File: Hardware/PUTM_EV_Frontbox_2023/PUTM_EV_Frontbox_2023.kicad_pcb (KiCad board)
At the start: 4 copper layers, 75 x 75 mm, 201 parts, among them IC1 ELVH-MF12D-HRRJ-C-N3A4, IC2 ELVH-MF12D-HRRJ-C-N3A4, J2 Conn_01x04, J5 Conn_02x14_Counter_Clockwise, K1 UMS05-1A80-75D, Q1 NX7002AK, SW1 Reset switch, U1 STM32G473RCTx, U10 TLP291-4, U11 TLP291-4, U12 TLV9152IDDFR, U17 MCP6002-xMC, U18 MCP6N11-005, U19 TLV743P, U2 MCP6002-xMC, U20 LM4040DBZ-5, U21 MCP6001, U22 MCP6N11-005, U23 MCP6001, U3 IMS330DHCX, U4 TLV743P, U5 TLV743P, U6 BD50FC0FP, U7 LM62440-Q1, U8 MCP2542FDxMF, Y1 ABM8G-48.000MHZ

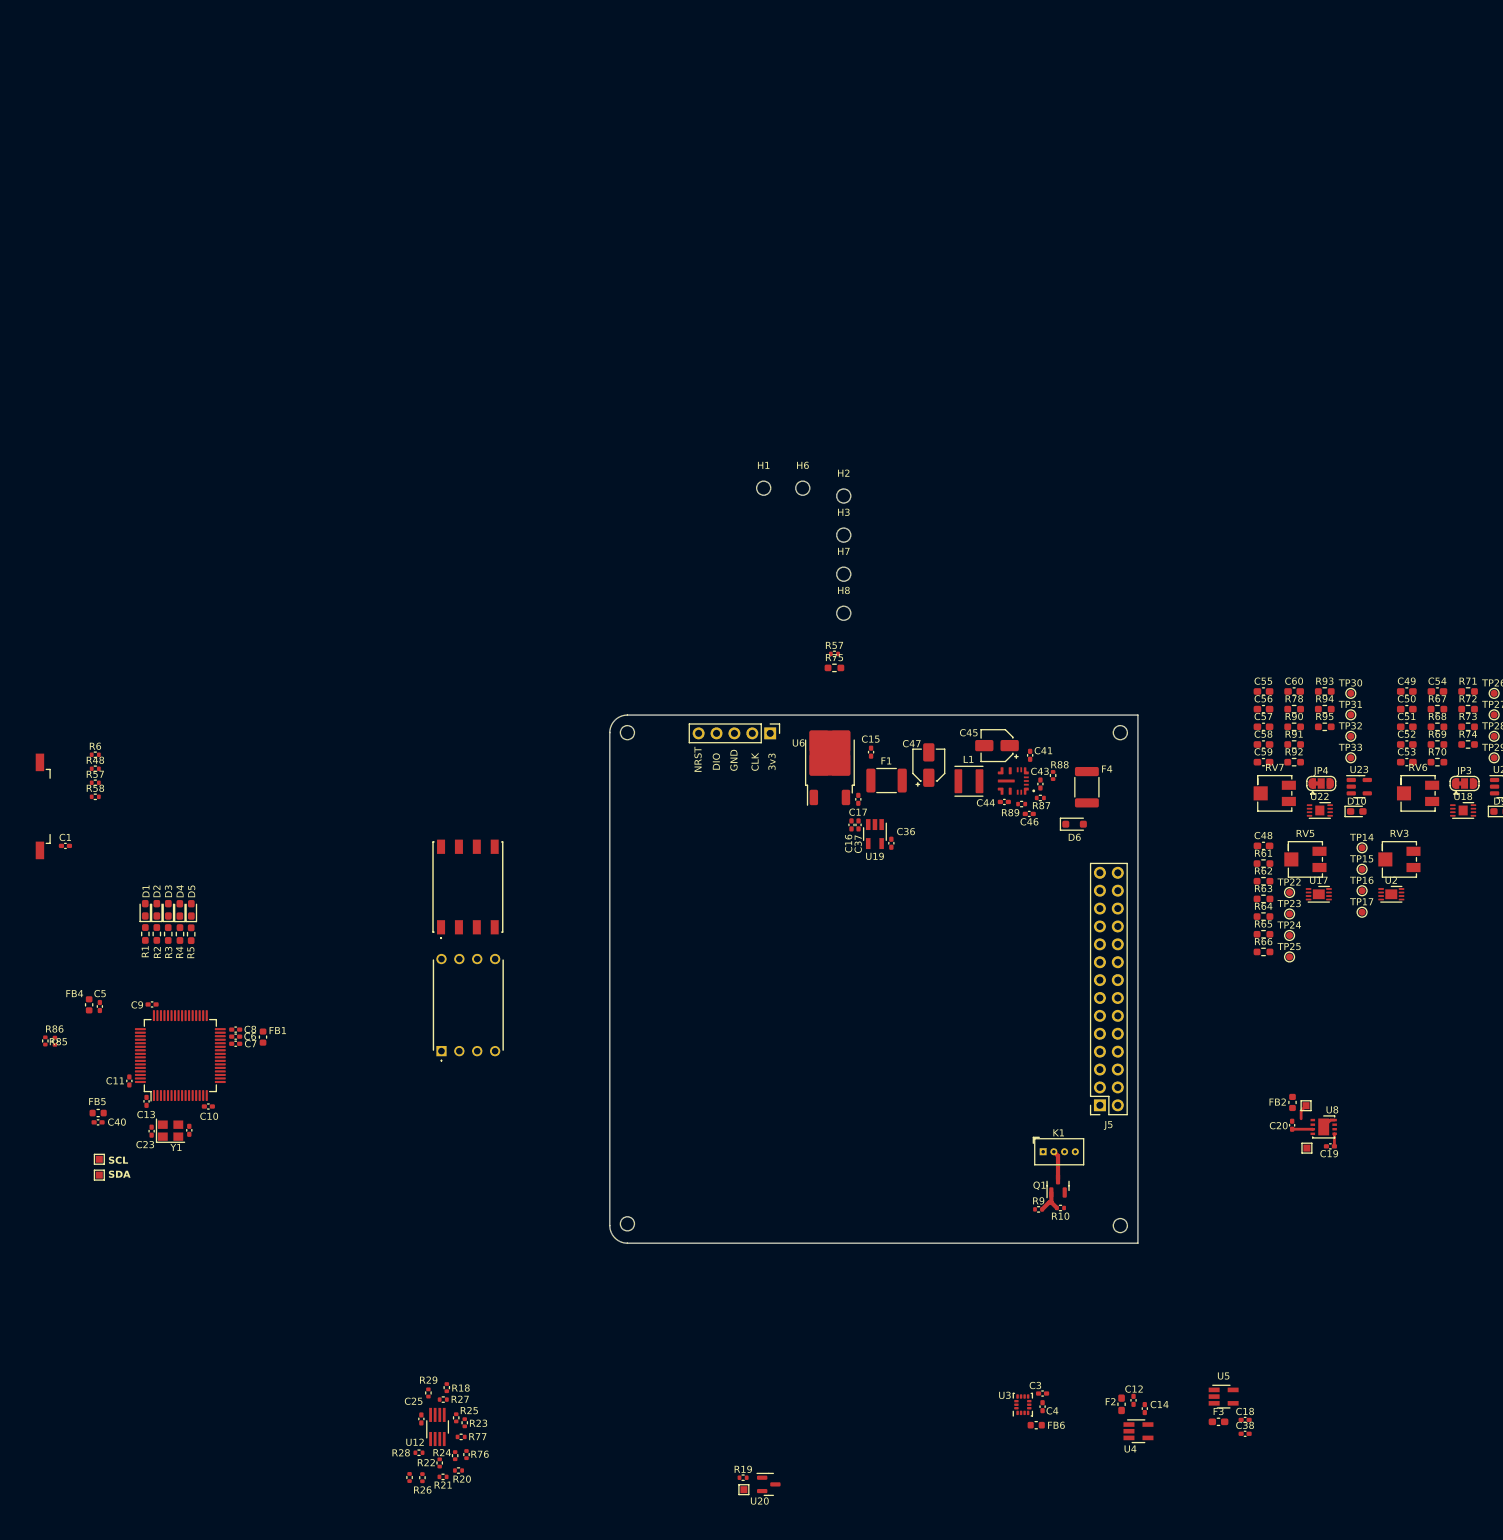
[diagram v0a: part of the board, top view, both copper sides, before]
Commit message: Schematic updates
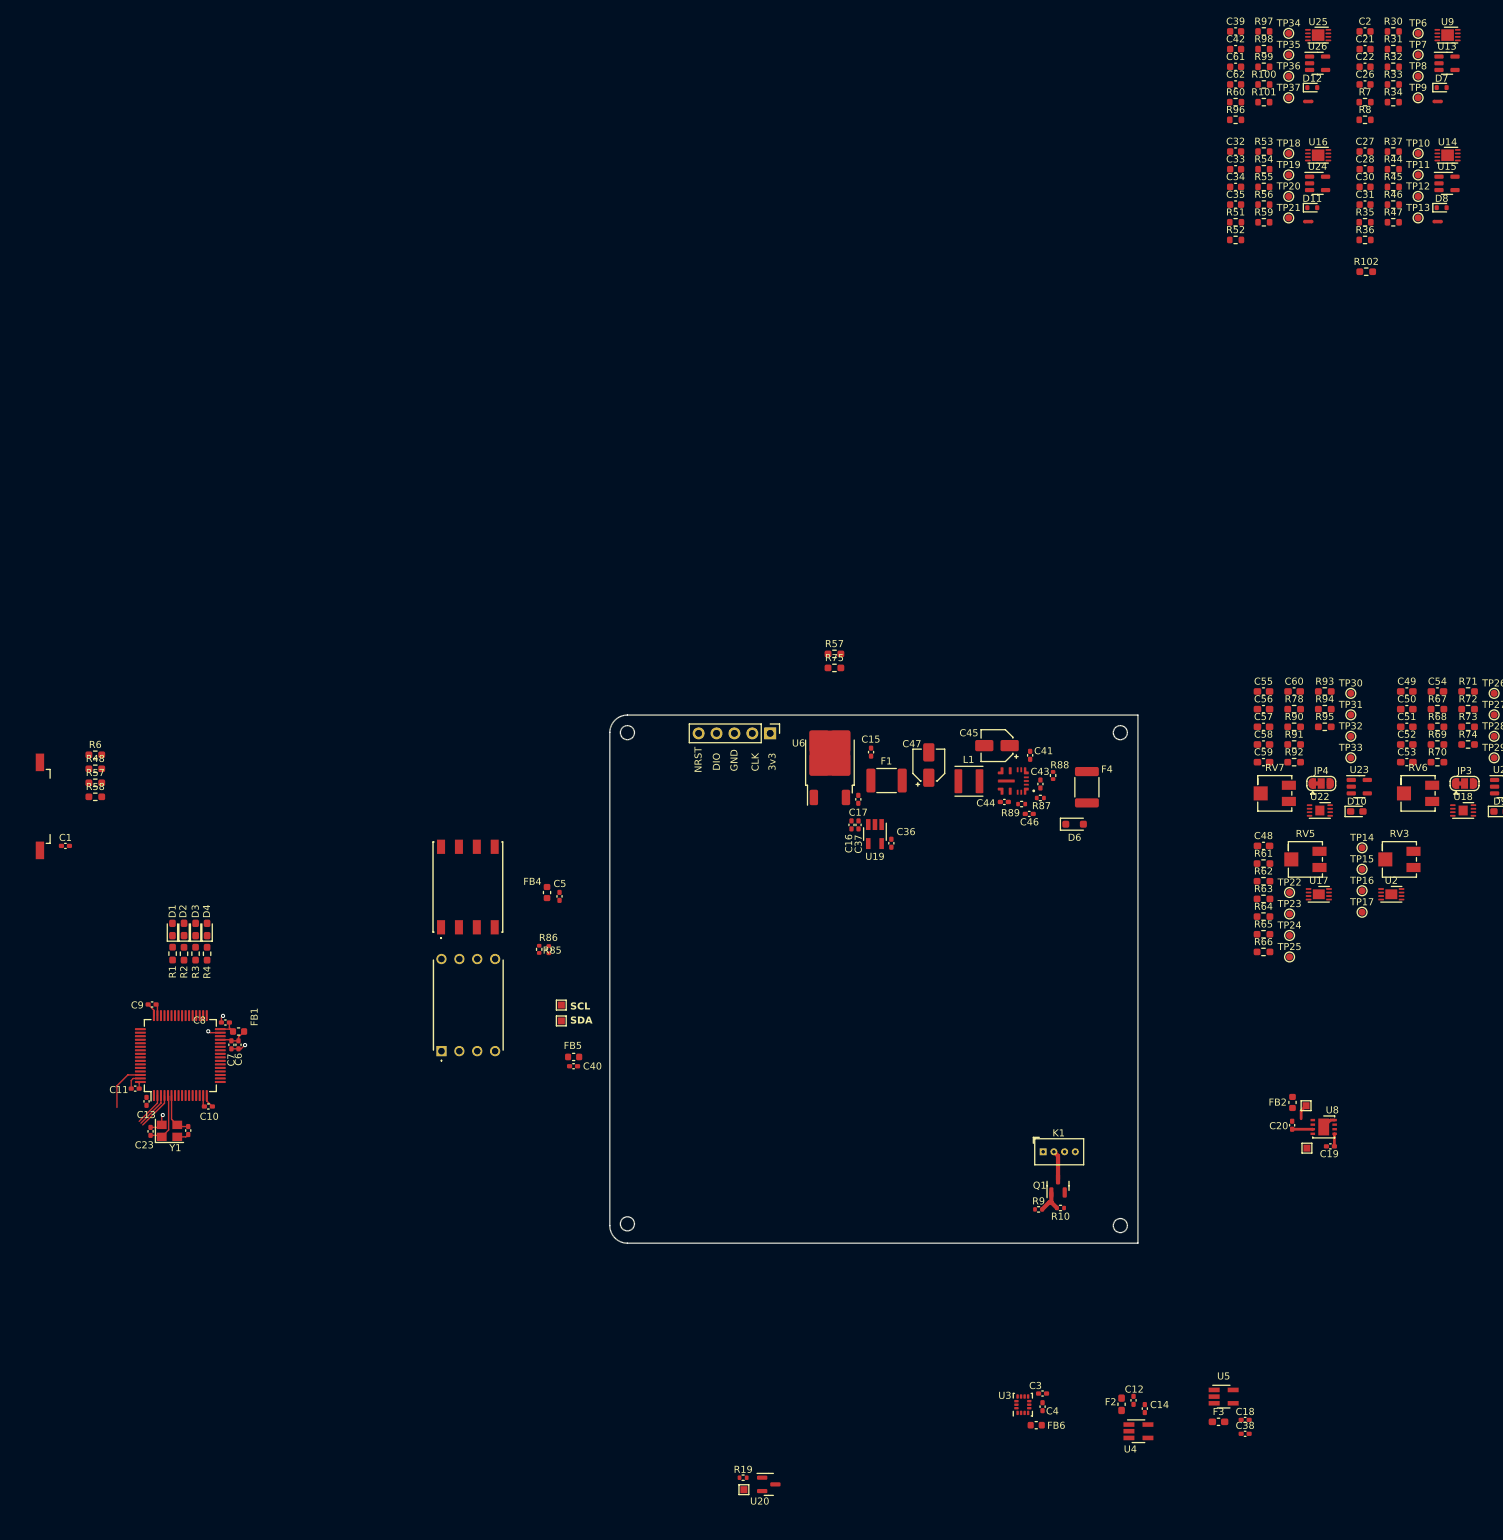
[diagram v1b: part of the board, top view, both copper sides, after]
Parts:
- removed C25: 100n, Capacitor_SMD:C_0402_1005Metric_Pad0.74x0.62mm_HandSolder
- removed D5: LED, Diode_SMD:D_0603_1608Metric_Pad1.05x0.95mm_HandSolder
- removed H1, H2, H3, H6, H7, H8: M3, MountingHole:MountingHole_2mm
- removed J5: Conn_02x14_Counter_Clockwise, Connector_PinSocket_2.54mm:PinSocket_2x14_P2.54mm_Vertical
- removed R17, R18: 5k, Resistor_SMD:R_0402_1005Metric
- removed R20, R21, R76, R77: 10k, Resistor_SMD:R_0402_1005Metric
- removed R22, R23, R26, R27: 3k, Resistor_SMD:R_0402_1005Metric
- removed R24, R25, R28, R29: 12k, Resistor_SMD:R_0402_1005Metric
- removed R5: 100R, Resistor_SMD:R_0603_1608Metric_Pad0.98x0.95mm_HandSolder
- removed U12: TLV9152IDDFR, Package_TO_SOT_SMD:TSOT-23-8_HandSoldering
- added C2: 100n, Capacitor_SMD:C_0603_1608Metric, F.Cu at (232.2, -47.1)
- added C21: 100n, Capacitor_SMD:C_0603_1608Metric, F.Cu at (232.2, -44.6)
- added C22: 100n, Capacitor_SMD:C_0603_1608Metric, F.Cu at (232.2, -42.1)
- added C26: 100n, Capacitor_SMD:C_0603_1608Metric, F.Cu at (232.2, -39.5)
- added C27: 100n, Capacitor_SMD:C_0603_1608Metric, F.Cu at (232.2, -30.0)
- added C28: 100n, Capacitor_SMD:C_0603_1608Metric, F.Cu at (232.2, -27.5)
- added C30: 100n, Capacitor_SMD:C_0603_1608Metric, F.Cu at (232.2, -25.0)
- added C31: 100n, Capacitor_SMD:C_0603_1608Metric, F.Cu at (232.2, -22.5)
- added C32: 100n, Capacitor_SMD:C_0603_1608Metric, F.Cu at (213.9, -30.0)
- added C33: 100n, Capacitor_SMD:C_0603_1608Metric, F.Cu at (213.9, -27.5)
- added C34: 100n, Capacitor_SMD:C_0603_1608Metric, F.Cu at (213.9, -25.0)
- added C35: 100n, Capacitor_SMD:C_0603_1608Metric, F.Cu at (213.9, -22.5)
- added C39: 100n, Capacitor_SMD:C_0603_1608Metric, F.Cu at (213.9, -47.1)
- added C42: 100n, Capacitor_SMD:C_0603_1608Metric, F.Cu at (213.9, -44.6)
- added C61: 100n, Capacitor_SMD:C_0603_1608Metric, F.Cu at (213.9, -42.1)
- added C62: 100n, Capacitor_SMD:C_0603_1608Metric, F.Cu at (213.9, -39.5)
- added D11: 5V, Diode_SMD:D_SOD-523, F.Cu at (224.8, -22.1)
- added D12: 5V, Diode_SMD:D_SOD-523, F.Cu at (224.8, -39.1)
- added D7: 5V, Diode_SMD:D_SOD-523, F.Cu at (243.1, -39.1)
- added D8: 5V, Diode_SMD:D_SOD-523, F.Cu at (243.1, -22.1)
- added NT1: NetTie_2, NetTie:NetTie-2_SMD_Pad0.5mm, F.Cu at (242.6, -37.1)
- added NT2: NetTie_2, NetTie:NetTie-2_SMD_Pad0.5mm, F.Cu at (242.6, -20.1)
- added NT3: NetTie_2, NetTie:NetTie-2_SMD_Pad0.5mm, F.Cu at (224.2, -20.1)
- added NT4: NetTie_2, NetTie:NetTie-2_SMD_Pad0.5mm, F.Cu at (224.2, -37.1)
- added R100: 3k3, Resistor_SMD:R_0603_1608Metric, F.Cu at (217.9, -39.5)
- added R101: 3k3, Resistor_SMD:R_0603_1608Metric, F.Cu at (217.9, -37.0)
- added R102: 10k, Resistor_SMD:R_0603_1608Metric_Pad0.98x0.95mm_HandSolder, F.Cu at (232.4, -13.0)
- added R30: 5k, Resistor_SMD:R_0603_1608Metric, F.Cu at (236.3, -47.1)
- added R31: TBD, Resistor_SMD:R_0603_1608Metric, F.Cu at (236.3, -44.6)
- added R32: TBD, Resistor_SMD:R_0603_1608Metric, F.Cu at (236.3, -42.1)
- added R33: 3k3, Resistor_SMD:R_0603_1608Metric, F.Cu at (236.3, -39.5)
- added R34: 3k3, Resistor_SMD:R_0603_1608Metric, F.Cu at (236.3, -37.0)
- added R35: 50k, Resistor_SMD:R_0603_1608Metric, F.Cu at (232.2, -20.0)
- added R36: 50k, Resistor_SMD:R_0603_1608Metric, F.Cu at (232.2, -17.5)
- added R37: 5k, Resistor_SMD:R_0603_1608Metric, F.Cu at (236.3, -30.0)
- added R44: TBD, Resistor_SMD:R_0603_1608Metric, F.Cu at (236.3, -27.5)
- added R45: TBD, Resistor_SMD:R_0603_1608Metric, F.Cu at (236.3, -25.0)
- added R46: 3k3, Resistor_SMD:R_0603_1608Metric, F.Cu at (236.3, -22.5)
- added R47: 3k3, Resistor_SMD:R_0603_1608Metric, F.Cu at (236.3, -20.0)
- added R51: 50k, Resistor_SMD:R_0603_1608Metric, F.Cu at (213.9, -20.0)
- added R52: 50k, Resistor_SMD:R_0603_1608Metric, F.Cu at (213.9, -17.5)
- added R53: 5k, Resistor_SMD:R_0603_1608Metric, F.Cu at (217.9, -30.0)
- added R54: TBD, Resistor_SMD:R_0603_1608Metric, F.Cu at (217.9, -27.5)
- added R55: TBD, Resistor_SMD:R_0603_1608Metric, F.Cu at (217.9, -25.0)
- added R56: 3k3, Resistor_SMD:R_0603_1608Metric, F.Cu at (217.9, -22.5)
- added R59: 3k3, Resistor_SMD:R_0603_1608Metric, F.Cu at (217.9, -20.0)
- added R60: 50k, Resistor_SMD:R_0603_1608Metric, F.Cu at (213.9, -37.0)
- added R7: 50k, Resistor_SMD:R_0603_1608Metric, F.Cu at (232.2, -37.0)
- added R8: 50k, Resistor_SMD:R_0603_1608Metric, F.Cu at (232.2, -34.5)
- added R96: 50k, Resistor_SMD:R_0603_1608Metric, F.Cu at (213.9, -34.5)
- added R97: 5k, Resistor_SMD:R_0603_1608Metric, F.Cu at (217.9, -47.1)
- added R98: TBD, Resistor_SMD:R_0603_1608Metric, F.Cu at (217.9, -44.6)
- added R99: TBD, Resistor_SMD:R_0603_1608Metric, F.Cu at (217.9, -42.1)
- added TP10: TestPoint_Small, TestPoint:TestPoint_Pad_D1.0mm, F.Cu at (239.8, -29.8)
- added TP11: TestPoint_Small, TestPoint:TestPoint_Pad_D1.0mm, F.Cu at (239.8, -26.7)
- added TP12: TestPoint_Small, TestPoint:TestPoint_Pad_D1.0mm, F.Cu at (239.8, -23.6)
- added TP13: TestPoint_Small, TestPoint:TestPoint_Pad_D1.0mm, F.Cu at (239.8, -20.6)
- added TP18: TestPoint_Small, TestPoint:TestPoint_Pad_D1.0mm, F.Cu at (221.4, -29.8)
- added TP19: TestPoint_Small, TestPoint:TestPoint_Pad_D1.0mm, F.Cu at (221.4, -26.7)
- added TP20: TestPoint_Small, TestPoint:TestPoint_Pad_D1.0mm, F.Cu at (221.4, -23.6)
- added TP21: TestPoint_Small, TestPoint:TestPoint_Pad_D1.0mm, F.Cu at (221.4, -20.6)
- added TP34: TestPoint_Small, TestPoint:TestPoint_Pad_D1.0mm, F.Cu at (221.4, -46.8)
- added TP35: TestPoint_Small, TestPoint:TestPoint_Pad_D1.0mm, F.Cu at (221.4, -43.8)
- added TP36: TestPoint_Small, TestPoint:TestPoint_Pad_D1.0mm, F.Cu at (221.4, -40.7)
- added TP37: TestPoint_Small, TestPoint:TestPoint_Pad_D1.0mm, F.Cu at (221.4, -37.7)
- added TP6: TestPoint_Small, TestPoint:TestPoint_Pad_D1.0mm, F.Cu at (239.8, -46.8)
- added TP7: TestPoint_Small, TestPoint:TestPoint_Pad_D1.0mm, F.Cu at (239.8, -43.8)
- added TP8: TestPoint_Small, TestPoint:TestPoint_Pad_D1.0mm, F.Cu at (239.8, -40.7)
- added TP9: TestPoint_Small, TestPoint:TestPoint_Pad_D1.0mm, F.Cu at (239.8, -37.7)
- added U13: MCP6001, Package_TO_SOT_SMD:SOT-23-5, F.Cu at (243.9, -42.6)
- added U14: MCP6N11-005, Package_DFN_QFN:TDFN-8-1EP_3x2mm_P0.5mm_EP1.80x1.65mm, F.Cu at (244.0, -29.5)
- added U15: MCP6001, Package_TO_SOT_SMD:SOT-23-5, F.Cu at (243.9, -25.5)
- added U16: MCP6N11-005, Package_DFN_QFN:TDFN-8-1EP_3x2mm_P0.5mm_EP1.80x1.65mm, F.Cu at (225.6, -29.5)
- added U24: MCP6001, Package_TO_SOT_SMD:SOT-23-5, F.Cu at (225.5, -25.5)
- added U25: MCP6N11-005, Package_DFN_QFN:TDFN-8-1EP_3x2mm_P0.5mm_EP1.80x1.65mm, F.Cu at (225.6, -46.6)
- added U26: MCP6001, Package_TO_SOT_SMD:SOT-23-5, F.Cu at (225.5, -42.6)
- added U9: MCP6N11-005, Package_DFN_QFN:TDFN-8-1EP_3x2mm_P0.5mm_EP1.80x1.65mm, F.Cu at (244.0, -46.6)
- D1, D2, D3, D4: footprint Diode_SMD:D_0603_1608Metric_Pad1.05x0.95mm_HandSolder -> LED_SMD:LED_0603_1608Metric_Pad1.05x0.95mm_HandSolder
- R48, R57 (x2), R58, R6: footprint Resistor_SMD:R_0402_1005Metric -> Resistor_SMD:R_0603_1608Metric_Pad0.98x0.95mm_HandSolder
- moved R85 71.3 mm to (115.0, 83.3)
- moved R86 71.3 mm to (116.3, 83.3)
- moved TP4 69.2 mm to (118.1, 91.2)
- moved TP5 69.2 mm to (118.1, 93.4)
- moved C40 68.0 mm to (119.9, 99.9)
- moved FB5 68.0 mm to (119.9, 98.6)
- moved C5 67.1 mm to (117.9, 75.8)
- moved FB4 66.9 mm to (116.1, 75.2)
- moved R3 4.78 mm to (66.2, 83.9), turned to -90 degrees
- moved D3 4.77 mm to (66.2, 80.5)
- moved R2 4.77 mm to (64.5, 83.9), turned to -90 degrees
- moved D2 4.77 mm to (64.5, 80.4)
- moved R1 4.77 mm to (62.9, 83.9), turned to -90 degrees
- moved D4 4.77 mm to (67.8, 80.5)
- moved D1 4.77 mm to (62.9, 80.5)
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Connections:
- R39 pad 2: /BRAKE_PRESSURE1 -> /BRAKE_PRESSURE1_IN
- R43 pad 1: /Brake_press_front -> /BRAKE_PRESSURE_FRONT_OUT
- R57 pad 1: Net-(U5-OUT) -> Net-(J1-Pin_23)
- R57 pad 2: /APPS2_3V3 -> GND
- R57 pad 1: Net-(J5-Pin_19) -> Net-(J1-Pin_23)
- R62 pad 2: /BRAKE_PRESSURE2 -> /BRAKE_PRESSURE2_IN
- R66 pad 1: /Brake_press_rear -> /BRAKE_PRESSURE_REAR_OUT
- TP17 pad 1: /Brake_press_front -> /BRAKE_PRESSURE_FRONT_OUT
- TP25 pad 1: /Brake_press_rear -> /BRAKE_PRESSURE_REAR_OUT
- U1 pad 19: unconnected-(U1-PA5-Pad19) -> /DAC2_REF
- U1 pad 20: /SUSP_L -> /DAC1_REF
- U1 pad 21: /SUSP_R -> /SUSP_R_OUT
- U1 pad 22: /Brake_pressure_front -> /SUSP_L_OUT
- U1 pad 23: /Brake_pressure_rear -> /BRAKE_PRESSURE_REAR_OUT
- U1 pad 24: unconnected-(U1-PB0-Pad24) -> /BRAKE_PRESSURE_FRONT_OUT
- U1 pad 25: unconnected-(U1-PB1-Pad25) -> /BRAKE_POSITION_OUT
- U1 pad 26: unconnected-(U1-PB2-Pad26) -> /STEERING_POSITION_OUT
- U1 pad 3: /RTD_BUTTON_sig -> unconnected-(U1-PC14-Pad3)
- U1 pad 43: /DEBUG_LED5 -> unconnected-(U1-PA9-Pad43)
- U1 pad 44: /DAC1_REF -> unconnected-(U1-PA10-Pad44)
- U1 pad 52: /DAC2_REF -> unconnected-(U1-PC10-Pad52)
- U17 pad 1: /Brake_press_rear -> /BRAKE_PRESSURE_REAR_OUT
- U2 pad 1: /Brake_press_front -> /BRAKE_PRESSURE_FRONT_OUT
- U8 pad 6: /CAN- -> /CAN2-
- U8 pad 7: /CAN+ -> /CAN1+
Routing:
- net GND: track 2.41 -> 18.5 mm, vias 0 -> 4
- net +3.3V: track 1.80 -> 10.1 mm
- net /HSE_IN: track 0.00 -> 7.99 mm
- net /Sense_BSPD: track 0.00 -> 7.03 mm
- net /HSE_OUT: track 0.38 -> 6.16 mm
- net /Sense_EBS: track 0.00 -> 5.45 mm
- net unconnected-(U1-PC14-Pad3): track 0.00 -> 5.09 mm
- net /Sense_overtravel: track 0.00 -> 4.74 mm
- net +3.3VA: track 0.00 -> 4.30 mm

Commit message: Started PCB layout
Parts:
- removed D12: 5V, Diode_SMD:D_SOD-523
- removed F1: 1A, Fuse:Fuse_1812_4532Metric_Pad1.30x3.40mm_HandSolder
- removed H10, H4, H5, H9: M3, MountingHole:MountingHole_2mm
- removed NT1, NT2, NT3, NT4: NetTie_2, NetTie:NetTie-2_SMD_Pad0.5mm
- removed R100, R101, R56, R59: 3k3, Resistor_SMD:R_0603_1608Metric
- removed R102: 10k, Resistor_SMD:R_0603_1608Metric_Pad0.98x0.95mm_HandSolder
- removed R52, R60, R96: 50k, Resistor_SMD:R_0603_1608Metric
- removed R53, R97: 5k, Resistor_SMD:R_0603_1608Metric
- removed R54, R55, R98, R99: TBD, Resistor_SMD:R_0603_1608Metric
- removed the R57 at (156.9, 41.3)
- added C25: 100nF, Capacitor_SMD:C_0402_1005Metric_Pad0.74x0.62mm_HandSolder, F.Cu at (161.8, 53.1)
- added C63: 100nF, Capacitor_SMD:C_0402_1005Metric_Pad0.74x0.62mm_HandSolder, F.Cu at (160.2, 57.0)
- added D5: 5V, Diode_SMD:D_SOD-523, F.Cu at (362.3, 106.3)
- added FB3: 60R@100MHz, Inductor_SMD:L_0603_1608Metric, F.Cu at (159.0, 57.4)
- added H1: MountingHole_Pad, MountingHole:MountingHole_3.2mm_M3_DIN965_Pad_TopBottom, F.Cu at (196.6, 104.5)
- added H2: MountingHole_Pad, MountingHole:MountingHole_3.2mm_M3_DIN965_Pad_TopBottom, F.Cu at (196.6, 53.4)
- added J1: Conn_02x16_Counter_Clockwise, Connector_PinHeader_2.54mm:PinHeader_2x16_P2.54mm_Vertical, F.Cu at (195.7, 98.0)
- added R17: TBD, Resistor_SMD:R_0603_1608Metric, F.Cu at (359.5, 102.1)
- added R18: TBD, Resistor_SMD:R_0603_1608Metric, F.Cu at (359.5, 100.5)
- added R20: 3k3, Resistor_SMD:R_0603_1608Metric, F.Cu at (362.6, 102.1)
- added R21: 3k3, Resistor_SMD:R_0603_1608Metric, F.Cu at (362.6, 100.5)
- added R22: 50k, Resistor_SMD:R_0603_1608Metric, F.Cu at (323.6, 106.8)
- added R23: 50k, Resistor_SMD:R_0603_1608Metric, F.Cu at (323.6, 108.4)
- added R24: 5k, Resistor_SMD:R_0603_1608Metric, F.Cu at (326.6, 108.4)
- added R25: TBD, Resistor_SMD:R_0603_1608Metric, F.Cu at (323.6, 102.6)
- added R26: TBD, Resistor_SMD:R_0603_1608Metric, F.Cu at (323.6, 101.1)
- added R27: 3k3, Resistor_SMD:R_0603_1608Metric, F.Cu at (326.6, 102.6)
- added R28: 3k3, Resistor_SMD:R_0603_1608Metric, F.Cu at (326.6, 101.1)
- added R29: 50k, Resistor_SMD:R_0603_1608Metric, F.Cu at (342.3, 107.0)
- added R5: 50k, Resistor_SMD:R_0603_1608Metric, F.Cu at (359.5, 106.3)
- added TP38: TestPoint, TestPoint:TestPoint_Pad_1.0x1.0mm, F.Cu at (169.0, 34.6)
- added TP39: TestPoint, TestPoint:TestPoint_Pad_1.0x1.0mm, F.Cu at (168.9, 30.1)
- added U12: MCP2542FDxMF, Package_DFN_QFN:DFN-8-1EP_3x3mm_P0.65mm_EP1.55x2.4mm, F.Cu at (159.5, 53.7)
- C26, C31, C35, C62: footprint Capacitor_SMD:C_0603_1608Metric -> Capacitor_SMD:C_0402_1005Metric_Pad0.74x0.62mm_HandSolder
- R30: value 5k -> 50k
- R31: value TBD -> 5k
- R33: value 3k3 -> TBD
- R51: value 50k -> 3k3
- R8: value 50k -> 5k
- moved R38 221.4 mm to (238.4, 133.8), turned to -90 degrees
- moved C29 218.8 mm to (236.9, 127.8), turned to 90 degrees
- moved R40 218.3 mm to (236.9, 133.8), turned to 90 degrees
- moved R39 217.6 mm to (235.3, 133.8), turned to -90 degrees
- moved R41 217.2 mm to (238.4, 127.8), turned to 90 degrees
- moved R43 212.8 mm to (235.3, 127.8), turned to 90 degrees
- moved R42 212.0 mm to (233.8, 127.8), turned to 90 degrees
- moved TP34 201.4 mm to (346.4, 111.2), turned to -90 degrees
- moved TP6 200.1 mm to (363.5, 110.4), turned to -90 degrees
- moved TP35 197.2 mm to (343.3, 111.2), turned to -90 degrees
- moved C62 196.1 mm to (346.6, 104.7), turned to 90 degrees
- moved TP7 195.8 mm to (360.5, 110.4), turned to -90 degrees
- moved C42 195.3 mm to (345.4, 99.8)
- moved C39 195.1 mm to (342.3, 99.8), turned to 180 degrees
- moved C26 194.7 mm to (363.8, 104.0), turned to 90 degrees
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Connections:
- net /APPS_POT_2 renamed /APPS2/POT1
- net /Brake Position Potentiometer/IN+ renamed /Steering Position/IN+
- C15 pad 1: Net-(U6-VCC) -> +7.5V
- C21 pad 2: /SUSP_R_OUT -> /BRAKE_POSITION_OUT
- C33 pad 2: /BRAKE_POSITION_OUT -> /STEERING_POSITION_OUT
- C42 pad 2: /STEERING_POSITION_OUT -> /SUSP_R_OUT
- C49 pad 1: 3V3_POT1 -> /APPS1/3V3_POT2
- C50 pad 1: 3V3_POT1 -> /APPS1/3V3_POT2
- C54 pad 2: /APPS1/OUT2 -> /APPS_sig1
- C55 pad 1: 3V3_POT1 -> /APPS2/3V3_POT1
- C56 pad 1: 3V3_POT1 -> /APPS2/3V3_POT1
- C58 pad 1: /DAC2_REF -> /APPS2/DAC_REF1
- D11 pad 2: /Brake Position Potentiometer/IN- -> /SUSPENSION_POT2_IN
- D7 pad 2: /Suspension Potentiometer (Right)/IN- -> /STEERING_POSITION_IN
- D8 pad 2: /Suspension Potentiometer (Left)/IN- -> /SUSPENSION_POT1_IN
- JP4 pad 1: /DAC2_REF -> /APPS2/DAC_REF1
- R30 pad 1: /Suspension Potentiometer (Right)/IN+ -> +5V_EXT
- R30 pad 2: GND -> /Suspension Potentiometer (Right)/IN+
- R31 pad 1: Net-(U9-FG) -> /Suspension Potentiometer (Right)/IN+
- R31 pad 2: Net-(R31-Pad2) -> GND
- R32 pad 1: GND -> Net-(U25-FG)
- R32 pad 2: Net-(U9-FG) -> Net-(R32-Pad2)
- R33 pad 1: Net-(R31-Pad2) -> GND
- R33 pad 2: Net-(C21-Pad1) -> Net-(U25-FG)
- R34 pad 1: Net-(C21-Pad1) -> Net-(R32-Pad2)
- R34 pad 2: Net-(U13-+) -> Net-(C42-Pad1)
- R35 pad 2: /Suspension Potentiometer (Left)/IN- -> /SUSPENSION_POT1_IN
- R51 pad 1: +5V_EXT -> Net-(C42-Pad1)
- R51 pad 2: /Brake Position Potentiometer/IN- -> Net-(U26-+)
- R57 pad 1: Net-(J1-Pin_23) -> GND
- R57 pad 2: GND -> Net-(J1-Pin_16)
- R58 pad 1: Net-(J1-Pin_22) -> GND
- R58 pad 2: GND -> Net-(J1-Pin_15)
- R67 pad 1: 3V3_POT1 -> /APPS1/3V3_POT2
- R7 pad 2: /Suspension Potentiometer (Right)/IN- -> /Brake Position/IN+
- R70 pad 2: 3V3_POT1 -> /APPS1/3V3_POT2
- R75 pad 1: 3V3_POT1 -> /APPS2/3V3_POT1
- R8 pad 1: +5V_EXT -> /Brake Position/IN+
- R8 pad 2: /Suspension Potentiometer (Right)/IN+ -> GND
- R91 pad 2: 3V3_POT1 -> /APPS2/3V3_POT1
- TP10 pad 1: /Suspension Potentiometer (Left)/IN- -> /SUSPENSION_POT1_IN
- TP18 pad 1: /Brake Position Potentiometer/IN- -> /STEERING_POSITION_IN
- TP21 pad 1: /BRAKE_POSITION_OUT -> /STEERING_POSITION_OUT
- TP29 pad 1: /APPS1/OUT2 -> /APPS_sig1
- TP34 pad 1: /Steering Wheel Angle/IN- -> /SUSPENSION_POT2_IN
- TP35 pad 1: /Steering Wheel Angle/IN+ -> /Suspension Potentiometer (Right)/IN+
- TP36 pad 1: Net-(R100-Pad1) -> Net-(R32-Pad2)
- TP37 pad 1: /STEERING_POSITION_OUT -> /SUSP_R_OUT
- TP6 pad 1: /Suspension Potentiometer (Right)/IN- -> /BRAKE_POSITION_IN
- TP7 pad 1: /Suspension Potentiometer (Right)/IN+ -> /Brake Position/IN+
- TP8 pad 1: Net-(R31-Pad2) -> Net-(R17-Pad2)
- TP9 pad 1: /SUSP_R_OUT -> /BRAKE_POSITION_OUT
- U13 pad 1: /SUSP_R_OUT -> /BRAKE_POSITION_OUT
- U13 pad 4: /SUSP_R_OUT -> /BRAKE_POSITION_OUT
- U14 pad 3: /Suspension Potentiometer (Left)/IN- -> /SUSPENSION_POT1_IN
- U16 pad 3: /Brake Position Potentiometer/IN- -> /STEERING_POSITION_IN
- U18 pad 7: 3V3_POT1 -> /APPS1/3V3_POT2
- U21 pad 1: /APPS1/OUT2 -> /APPS_sig1
- U21 pad 4: /APPS1/OUT2 -> /APPS_sig1
- U21 pad 5: 3V3_POT1 -> /APPS1/3V3_POT2
- U22 pad 7: 3V3_POT1 -> /APPS2/3V3_POT1
- U23 pad 5: 3V3_POT1 -> /APPS2/3V3_POT1
- U24 pad 1: /BRAKE_POSITION_OUT -> /STEERING_POSITION_OUT
- U24 pad 4: /BRAKE_POSITION_OUT -> /STEERING_POSITION_OUT
- U25 pad 2: /Steering Wheel Angle/IN+ -> /Suspension Potentiometer (Right)/IN+
- U25 pad 3: /Steering Wheel Angle/IN- -> /SUSPENSION_POT2_IN
- U25 pad 6: Net-(R100-Pad1) -> Net-(R32-Pad2)
- U26 pad 1: /STEERING_POSITION_OUT -> /SUSP_R_OUT
- U26 pad 4: /STEERING_POSITION_OUT -> /SUSP_R_OUT
- U6 pad 1: Net-(U6-VCC) -> +7.5V
- U8 pad 6: /CAN2- -> /CAN1-
- U9 pad 2: /Suspension Potentiometer (Right)/IN+ -> /Brake Position/IN+
- U9 pad 3: /Suspension Potentiometer (Right)/IN- -> /BRAKE_POSITION_IN
- U9 pad 6: Net-(R31-Pad2) -> Net-(R17-Pad2)
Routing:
- net GND: track 18.5 -> 101.1 mm, vias 4 -> 54
- net +3.3VA: track 4.30 -> 44.2 mm, vias 0 -> 12
- net +5V: track 0.00 -> 39.1 mm, vias 0 -> 9
- net /APPS2/DAC_REF1: track 0.00 -> 24.2 mm
- net +7.5V: track 0.00 -> 19.9 mm, vias 0 -> 2
- net /Brake Position/IN+: track 0.00 -> 19.7 mm
- net /APPS2/3V3_POT1: track 0.00 -> 18.3 mm, vias 0 -> 2
- net /APPS1/3V3_POT2: track 0.00 -> 18.3 mm, vias 0 -> 2
- net Net-(R17-Pad2): track 0.00 -> 18.2 mm
- net Net-(J1-Pin_17): track 0.00 -> 17.3 mm
- net /BRAKE_POSITION_IN: track 0.00 -> 16.6 mm
- net Net-(J1-Pin_15): track 0.00 -> 16.2 mm, vias 0 -> 1
- net /APPS1/DAC_REF2: track 0.00 -> 15.3 mm
- net /BRAKE_POSITION_OUT: track 0.00 -> 14.1 mm
- net Net-(J1-Pin_16): track 0.00 -> 13.6 mm, vias 0 -> 1
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- added copper zone on F.Cu, net +3.3V
- added copper zone on B.Cu, net +5V
- added copper zone on F.Cu, net +5V
- added copper zone on F.Cu, net +7.5V
- added copper zone on F.Cu, net GND
- added copper zone on F.Cu, net Net-(U7-EN)
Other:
- board size 75 x 75 mm -> 75 x 57.9 mm
